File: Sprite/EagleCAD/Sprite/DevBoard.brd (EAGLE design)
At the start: 35 x 35 mm, 31 parts, among them U1 CC430F5137, U2 HMC5883LSMD, U3 ITG-3200, X1 26 MHz

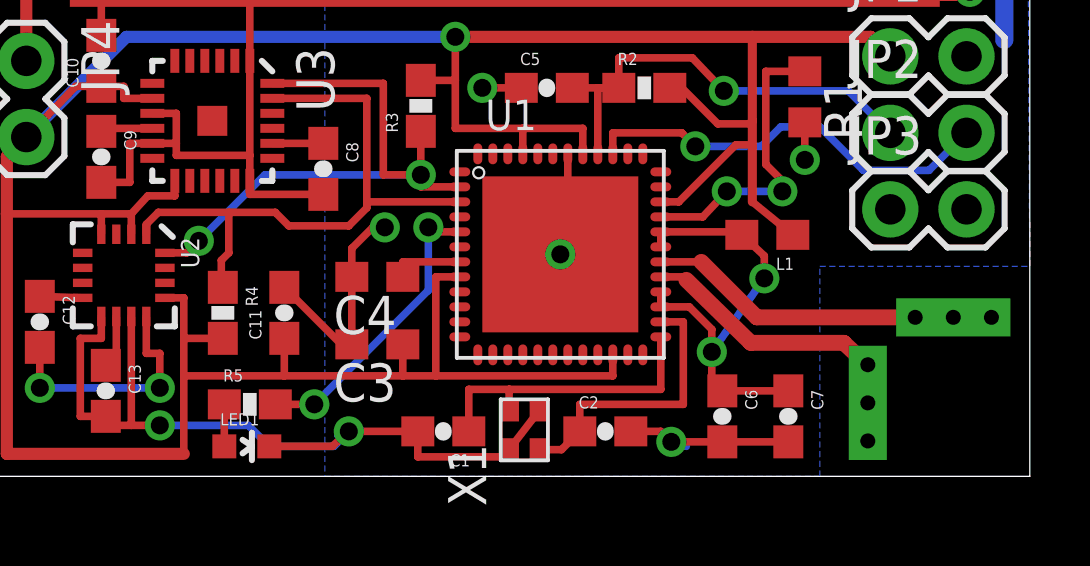
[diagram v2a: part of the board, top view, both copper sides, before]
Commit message: Connected serial pins on dev board
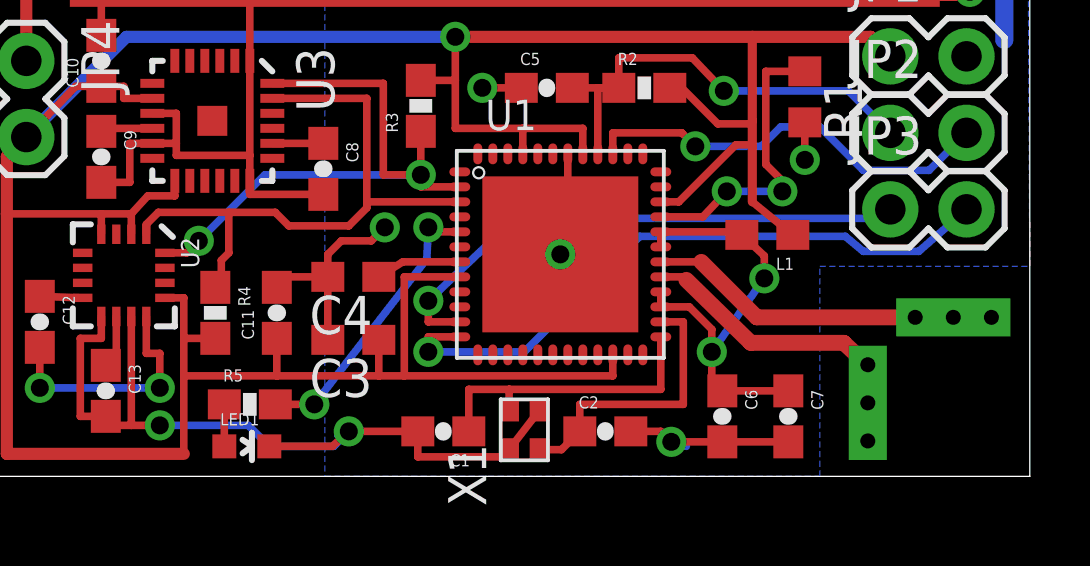
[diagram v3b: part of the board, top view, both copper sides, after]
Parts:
- moved C3 0.81 mm to (12.4, 4.55)
- moved C4 0.80 mm to (12.4, 6.65)
- moved C11 0.25 mm to (9.90, 5.45)
- moved R4 0.25 mm to (7.85, 5.45)
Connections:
- new net N$12: JP3.1, U1.11
- new net N$13: JP3.2, U1.12
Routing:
- net N$13: track 0.00 -> 21.8 mm, vias 0 -> 1
- net N$12: track 0.00 -> 18.4 mm, vias 0 -> 1
- net VCC: track 113.3 -> 114.3 mm
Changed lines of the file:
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@@
 <element name="C2" library="SparkFun" package="0603-CAP" value="27pF" x="20.85" y="1.5"/>
 <element name="R1" library="rcl" package="R0603" value="56K" x="27.5" y="12.65" rot="R270"/>
-<element name="C3" library="rcl" package="C0603" value="470nF" x="13.25" y="4.4" rot="R180"/>
-<element name="C4" library="rcl" package="C0603" value="470nF" x="13.25" y="6.65" rot="R180"/>
+<element name="C3" library="rcl" package="C0603" value="470nF" x="12.45" y="4.55" rot="R180"/>
+<element name="C4" library="rcl" package="C0603" value="470nF" x="12.45" y="6.65" rot="R180"/>
 <element name="U2" library="SparkFun" package="16LPCC" value="HMC5883LSMD" x="4.8" y="6.7" rot="R270"/>
-<element name="C11" library="SparkFun" package="0603-CAP" value="100nF" x="10.15" y="5.45" rot="R90"/>
+<element name="C11" library="SparkFun" package="0603-CAP" value="100nF" x="9.9" y="5.45" rot="R90"/>
 <element name="C12" library="SparkFun" package="0603-CAP" value="220nF" x="2" y="5.15" rot="R270"/>
 <element name="C13" library="SparkFun" package="0603-CAP" value="4.7uF" x="4.2" y="2.85" rot="R270"/>
@@
 <element name="C10" library="SparkFun" package="0603-CAP" value="10nF" x="4.05" y="13.85" rot="R90"/>
 <element name="R3" library="SparkFun" package="0603-RES" value="4.7K" x="14.7" y="12.35" rot="R90"/>
-<element name="R4" library="SparkFun" package="0603-RES" value="4.7K" x="8.1" y="5.45" rot="R270"/>
+<element name="R4" library="SparkFun" package="0603-RES" value="4.7K" x="7.85" y="5.45" rot="R270"/>
 <element name="JP2" library="SparkFun" package="1X02" value="" x="30.35" y="11.45"/>
 <element name="JP1" library="SparkFun" package="1X02" value="" x="30.35" y="14"/>
@@
 <wire x1="6.5" y1="9.85" x2="6.5" y2="9.35" width="0.254" layer="1"/>
 <contactref element="JP1" pad="1"/>
-<wire x1="8.1" y1="4.6" x2="6.8" y2="4.6" width="0.254" layer="1"/>
+<wire x1="7.85" y1="4.6" x2="6.8" y2="4.6" width="0.254" layer="1"/>
 <contactref element="U3" pad="8"/>
 <contactref element="C10" pad="1"/>
@@
 <contactref element="U1" pad="22"/>
 <contactref element="U1" pad="8"/>
-<wire x1="16" y1="6.65" x2="15.2" y2="6.65" width="0.254" layer="1"/>
-<wire x1="15.2" y1="6.65" x2="15.2" y2="3.35" width="0.254" layer="1"/>
+<wire x1="16" y1="6.65" x2="14.15" y2="6.65" width="0.254" layer="1"/>
+<wire x1="14.15" y1="6.65" x2="14.15" y2="3.35" width="0.254" layer="1"/>
 <wire x1="23" y1="12.95" x2="23.4" y2="12.95" width="0.254" layer="1"/>
 <wire x1="18.1" y1="10.75" x2="18.1" y2="11.6" width="0.254" layer="1"/>
@@
 <wire x1="20.1" y1="11.6" x2="18.1" y2="11.6" width="0.254" layer="1"/>
 <wire x1="21.1" y1="4.05" x2="21.1" y2="3.35" width="0.254" layer="1"/>
-<wire x1="21.1" y1="3.35" x2="15.2" y2="3.35" width="0.254" layer="1"/>
-<wire x1="14.1" y1="4.4" x2="14.1" y2="3.35" width="0.254" layer="1"/>
-<wire x1="14.1" y1="3.35" x2="15.2" y2="3.35" width="0.254" layer="1"/>
-<wire x1="6.8" y1="3.35" x2="10.15" y2="3.35" width="0.254" layer="1"/>
-<wire x1="10.15" y1="3.35" x2="10.15" y2="4.6" width="0.254" layer="1"/>
-<wire x1="14.1" y1="3.35" x2="10.15" y2="3.35" width="0.254" layer="1"/>
+<wire x1="21.1" y1="3.35" x2="14.15" y2="3.35" width="0.254" layer="1"/>
+<wire x1="13.3" y1="4.55" x2="13.3" y2="3.35" width="0.254" layer="1"/>
+<wire x1="13.3" y1="3.35" x2="14.15" y2="3.35" width="0.254" layer="1"/>
+<wire x1="6.8" y1="3.35" x2="9.9" y2="3.35" width="0.254" layer="1"/>
+<wire x1="9.9" y1="3.35" x2="9.9" y2="4.6" width="0.254" layer="1"/>
+<wire x1="13.3" y1="3.35" x2="9.9" y2="3.35" width="0.254" layer="1"/>
 <wire x1="23.4" y1="12.95" x2="24.6" y2="11.75" width="0.254" layer="1"/>
 <contactref element="L1" pad="1"/>
@@
 <via x="33" y="16.15" extent="1-16" drill="0.6"/>
 <via x="27.5" y="10.55" extent="1-16" drill="0.6"/>
-<wire x1="12.4" y1="4.4" x2="12.4" y2="6.65" width="0.254" layer="1"/>
+<wire x1="11.6" y1="4.55" x2="11.6" y2="6.65" width="0.254" layer="1"/>
 <via x="13.5" y="8.3" extent="1-16" drill="0.6"/>
 <wire x1="4.2" y1="2" x2="4.3" y2="1.7" width="0.254" layer="1"/>
@@
 <wire x1="19.6" y1="10.75" x2="19.6" y2="7.75" width="0.254" layer="1"/>
 <wire x1="19.6" y1="7.75" x2="19.35" y2="7.4" width="0.254" layer="1"/>
-<wire x1="12.4" y1="6.65" x2="12.4" y2="7.6" width="0.254" layer="1"/>
-<wire x1="12.4" y1="7.6" x2="13.1" y2="8.3" width="0.254" layer="1"/>
-<wire x1="13.1" y1="8.3" x2="13.5" y2="8.3" width="0.254" layer="1"/>
-<wire x1="12.4" y1="4.4" x2="12.05" y2="4.4" width="0.254" layer="1"/>
-<wire x1="12.05" y1="4.4" x2="10.15" y2="6.3" width="0.254" layer="1"/>
 <wire x1="14.6" y1="1.5" x2="12.3" y2="1.5" width="0.254" layer="1"/>
 <via x="12.3" y="1.5" extent="1-16" drill="0.6"/>
@@
 <wire x1="9" y1="16.15" x2="9" y2="16.05" width="0.254" layer="1"/>
 <wire x1="32.95" y1="16.15" x2="33" y2="16.15" width="0.6096" layer="1"/>
+<wire x1="11.6" y1="6.65" x2="9.9" y2="6.65" width="0.254" layer="1"/>
+<wire x1="9.9" y1="6.65" x2="9.9" y2="6.3" width="0.254" layer="1"/>
+<wire x1="11.6" y1="6.65" x2="11.6" y2="7.4" width="0.254" layer="1"/>
+<wire x1="11.6" y1="7.4" x2="12.05" y2="7.85" width="0.254" layer="1"/>
+<wire x1="12.05" y1="7.85" x2="13.05" y2="7.85" width="0.254" layer="1"/>
+<wire x1="13.05" y1="7.85" x2="13.5" y2="8.3" width="0.254" layer="1"/>
 <wire x1="32.89" y1="14" x2="34.15" y2="14.55" width="0" layer="19" extent="16-16"/>
+<wire x1="19.6" y1="10.75" x2="18.05" y2="12.95" width="0" layer="19" extent="1-1"/>
 </signal>
 <signal name="N$1">
@@
 <contactref element="C4" pad="1"/>
 <wire x1="16" y1="7.15" x2="14.1" y2="7.15" width="0.254" layer="1"/>
-<wire x1="14.1" y1="7.15" x2="14.1" y2="6.65" width="0.254" layer="1"/>
+<wire x1="14.1" y1="7.15" x2="13.3" y2="6.65" width="0.254" layer="1"/>
 </signal>
 <signal name="RFN">
@@
 <wire x1="9.85" y1="8.8" x2="10.3" y2="8.35" width="0.254" layer="1"/>
 <wire x1="10.3" y1="8.35" x2="12.3" y2="8.35" width="0.254" layer="1"/>
-<wire x1="8.1" y1="6.3" x2="8.05" y2="6.3" width="0.254" layer="1"/>
+<wire x1="7.85" y1="6.3" x2="8.05" y2="6.3" width="0.254" layer="1"/>
 <wire x1="8.05" y1="6.3" x2="8.05" y2="7.2" width="0.254" layer="1"/>
 <wire x1="8.05" y1="7.2" x2="8.3" y2="7.45" width="0.254" layer="1"/>
@@
 <wire x1="15.1" y1="8.15" x2="14.95" y2="8.3" width="0.254" layer="1"/>
 <via x="14.95" y="8.3" extent="1-16" drill="0.6"/>
-<wire x1="14.95" y1="8.3" x2="14.95" y2="6.2" width="0.254" layer="16"/>
-<wire x1="14.95" y1="6.2" x2="11.15" y2="2.4" width="0.254" layer="16"/>
+<wire x1="14.95" y1="8.3" x2="14.9" y2="7.25" width="0.254" layer="16"/>
+<wire x1="14.9" y1="7.25" x2="11.15" y2="2.4" width="0.254" layer="16"/>
 <via x="11.15" y="2.4" extent="1-16" drill="0.6"/>
 <wire x1="11.15" y1="2.4" x2="9.85" y2="2.4" width="0.254" layer="1"/>
@@
 <wire x1="17.5" y1="18.95" x2="17.5" y2="25" width="0.4064" layer="1"/>
 </signal>
+<signal name="N$12">
+<contactref element="JP3" pad="1"/>
+<contactref element="U1" pad="11"/>
+<wire x1="16" y1="5.15" x2="14.95" y2="5.15" width="0.254" layer="1"/>
+<wire x1="14.95" y1="5.15" x2="14.95" y2="5.85" width="0.254" layer="1"/>
+<via x="14.95" y="5.85" extent="1-16" drill="0.6"/>
+<wire x1="14.95" y1="5.85" x2="17.85" y2="8.6" width="0.254" layer="16"/>
+<wire x1="17.85" y1="8.6" x2="30.05" y2="8.6" width="0.254" layer="16"/>
+<wire x1="30.05" y1="8.6" x2="30.35" y2="8.9" width="0.254" layer="16"/>
+</signal>
+<signal name="N$13">
+<contactref element="JP3" pad="2"/>
+<contactref element="U1" pad="12"/>
+<wire x1="16" y1="4.65" x2="14.95" y2="4.65" width="0.254" layer="1"/>
+<wire x1="14.95" y1="4.65" x2="14.95" y2="4.15" width="0.254" layer="1"/>
+<via x="14.95" y="4.15" extent="1-16" drill="0.6"/>
+<wire x1="14.95" y1="4.15" x2="18.15" y2="4.15" width="0.254" layer="16"/>
+<wire x1="18.15" y1="4.15" x2="22" y2="8" width="0.254" layer="16"/>
+<wire x1="22" y1="8" x2="28.85" y2="8" width="0.254" layer="16"/>
+<wire x1="28.85" y1="8" x2="29.45" y2="7.5" width="0.254" layer="16"/>
+<wire x1="29.45" y1="7.5" x2="31.3" y2="7.5" width="0.254" layer="16"/>
+<wire x1="32.89" y1="8.9" x2="32.89" y2="8.89" width="0.254" layer="16"/>
+<wire x1="32.89" y1="8.89" x2="31.3" y2="7.5" width="0.254" layer="16"/>
+</signal>
 </signals>

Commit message: Programmer Board
Finished programmer shield board
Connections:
- net N$12 renamed RX
- net N$13 renamed TX
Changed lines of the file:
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@@
 <wire x1="17.5" y1="18.95" x2="17.5" y2="25" width="0.4064" layer="1"/>
 </signal>
-<signal name="N$12">
+<signal name="RX">
 <contactref element="JP3" pad="1"/>
 <contactref element="U1" pad="11"/>
@@
 <wire x1="30.05" y1="8.6" x2="30.35" y2="8.9" width="0.254" layer="16"/>
 </signal>
-<signal name="N$13">
+<signal name="TX">
 <contactref element="JP3" pad="2"/>
 <contactref element="U1" pad="12"/>
@@
 </signal>
 </signals>
-<errors>
-</errors>
 </board>
 </drawing>

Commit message: Finished Programmer Board
Added KickSat Silkscreen
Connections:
- net RX renamed TXD
- net TX renamed RXD
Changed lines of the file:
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@@
 <wire x1="17.5" y1="18.95" x2="17.5" y2="25" width="0.4064" layer="1"/>
 </signal>
-<signal name="RX">
+<signal name="TXD">
 <contactref element="JP3" pad="1"/>
 <contactref element="U1" pad="11"/>
@@
 <wire x1="30.05" y1="8.6" x2="30.35" y2="8.9" width="0.254" layer="16"/>
 </signal>
-<signal name="TX">
+<signal name="RXD">
 <contactref element="JP3" pad="2"/>
 <contactref element="U1" pad="12"/>
